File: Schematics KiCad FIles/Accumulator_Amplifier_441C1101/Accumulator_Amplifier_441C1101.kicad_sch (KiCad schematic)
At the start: 22 parts, among them J1 Edge, U1101 5963, U1105 5963

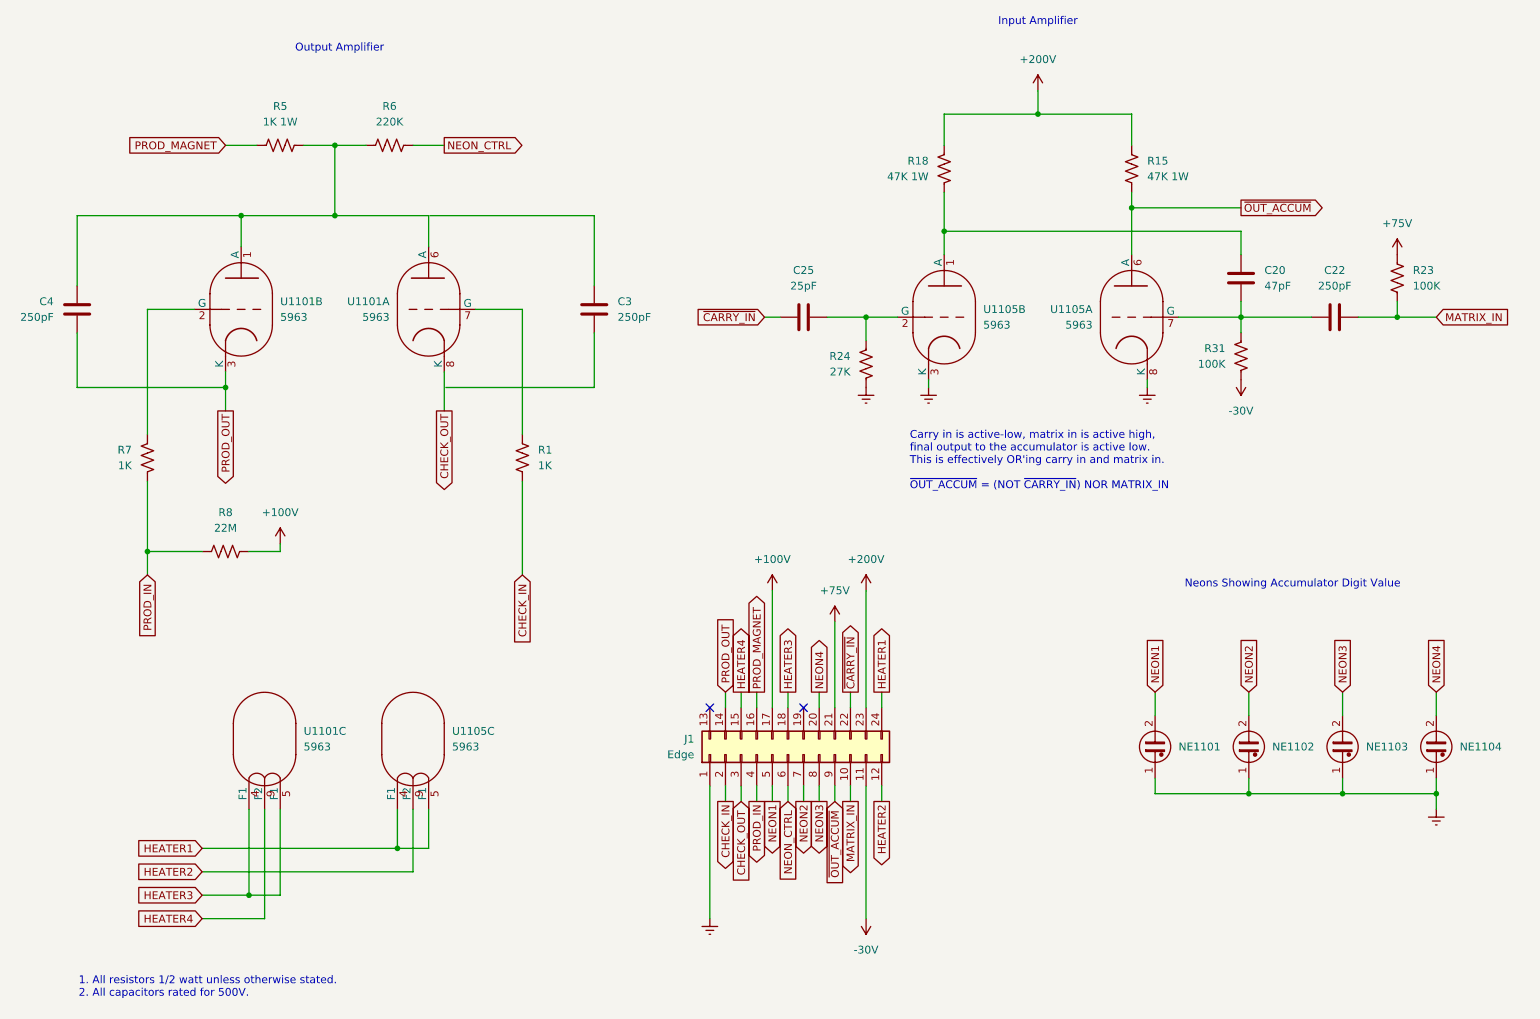
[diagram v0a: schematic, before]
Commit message: Fix component designators on accumulator schematics
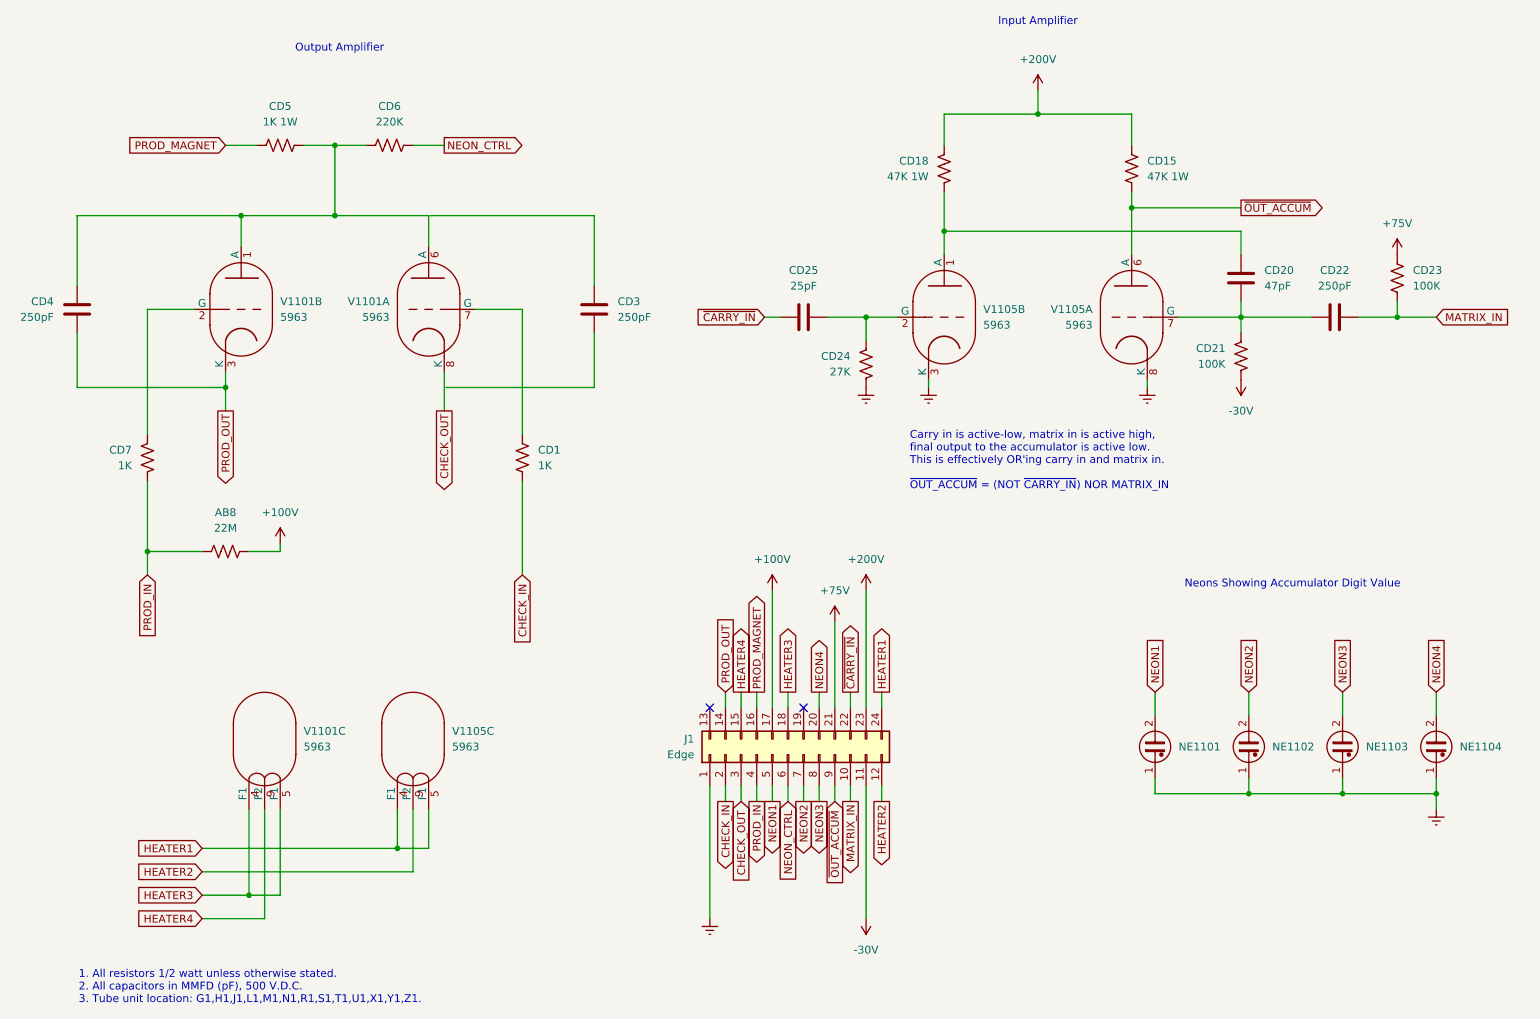
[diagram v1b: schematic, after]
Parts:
- renumbered R8 to AB8, R1 to CD1, R15 to CD15, R18 to CD18, C20 to CD20, R31 to CD21, C22 to CD22, R23 to CD23, R24 to CD24, C25 to CD25, C3 to CD3, C4 to CD4, R5 to CD5, R6 to CD6, R7 to CD7, U1101 to V1101, U1105 to V1105
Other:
- note added: "1. All resistors 1/2 watt unless otherwise stated. 2. All capacitors in MMFD (pF), 500 V.D.C. 3. Tube unit location: G1,H1,J1,L1,M1,N1,R1,S1,T1,U1,X1,Y1,Z1."
- note removed: "1. All resistors 1/2 watt unless otherwise stated. 2. All capacitors rated for 500V."
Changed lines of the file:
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@@
 		(title "Compu-Tronic Accumulator Amplifier Schematic")
 		(date "11-4-1958")
+		(comment 2 "For wiring diagram see 441E1102")
 	)
 	(junction
@@
 		)
 	)
-	(text "1. All resistors 1/2 watt unless otherwise stated.\n2. All capacitors rated for 500V."
+	(text "1. All resistors 1/2 watt unless otherwise stated.\n2. All capacitors in MMFD (pF), 500 V.D.C.\n3. Tube unit location: G1,H1,J1,L1,M1,N1,R1,S1,T1,U1,X1,Y1,Z1."
 		(exclude_from_sim no)
 		(at 32.004 178.816 0)
@@
 		(on_board yes)
 		(dnp no)
-		(property "Reference" "U1101"
+		(property "Reference" "V1101"
 			(at 82.55 67.3099 0)
 			(effects
@@
 			(project "Input_Amplifiier"
 				(path "/519d7692-6bf3-45ab-bd58-713783b63e8a"
-					(reference "U1101")
+					(reference "V1101")
 					(unit 1)
 				)
@@
 		(on_board yes)
 		(dnp no)
-		(property "Reference" "R23"
+		(property "Reference" "CD23"
 			(at 248.92 62.2299 0)
 			(effects
@@
 			(project "Accumulator_Amplifier_441C1101"
 				(path "/519d7692-6bf3-45ab-bd58-713783b63e8a"
-					(reference "R23")
+					(reference "CD23")
 					(unit 1)
 				)
@@
 		(dnp no)
 		(fields_autoplaced yes)
-		(property "Reference" "R8"
+		(property "Reference" "AB8"
 			(at 55.88 101.6 90)
 			(effects
@@
 			(project ""
 				(path "/519d7692-6bf3-45ab-bd58-713783b63e8a"
-					(reference "R8")
+					(reference "AB8")
 					(unit 1)
 				)
@@
 		(dnp no)
 		(fields_autoplaced yes)
-		(property "Reference" "R5"
+		(property "Reference" "CD5"
 			(at 64.77 35.56 90)
 			(effects
@@
 			(project "Accumulator_Amplifier_441C1101"
 				(path "/519d7692-6bf3-45ab-bd58-713783b63e8a"
-					(reference "R5")
+					(reference "CD5")
 					(unit 1)
 				)
@@
 		(on_board yes)
 		(dnp no)
-		(property "Reference" "C3"
+		(property "Reference" "CD3"
 			(at 119.634 67.3099 0)
 			(effects
@@
 			(project "Accumulator_Amplifier_441C1101"
 				(path "/519d7692-6bf3-45ab-bd58-713783b63e8a"
-					(reference "C3")
+					(reference "CD3")
 					(unit 1)
 				)
@@
 		(on_board yes)
 		(dnp no)
-		(property "Reference" "C20"
+		(property "Reference" "CD20"
 			(at 224.79 62.2299 0)
 			(effects
@@
 			(project "Accumulator_Amplifier_441C1101"
 				(path "/519d7692-6bf3-45ab-bd58-713783b63e8a"
-					(reference "C20")
+					(reference "CD20")
 					(unit 1)
 				)
@@
 		(on_board yes)
 		(dnp no)
-		(property "Reference" "R31"
+		(property "Reference" "CD21"
 			(at 218.44 74.9299 0)
 			(effects
@@
 			(project "Accumulator_Amplifier_441C1101"
 				(path "/519d7692-6bf3-45ab-bd58-713783b63e8a"
-					(reference "R31")
+					(reference "CD21")
 					(unit 1)
 				)
@@
 		(on_board yes)
 		(dnp no)
-		(property "Reference" "R7"
+		(property "Reference" "CD7"
 			(at 40.64 91.4399 0)
 			(effects
@@
 			(project ""
 				(path "/519d7692-6bf3-45ab-bd58-713783b63e8a"
-					(reference "R7")
+					(reference "CD7")
 					(unit 1)
 				)
@@
 		(dnp no)
 		(fields_autoplaced yes)
-		(property "Reference" "U1101"
+		(property "Reference" "V1101"
 			(at 68.58 137.1599 0)
 			(effects
@@
 			(project "Input_Amplifiier"
 				(path "/519d7692-6bf3-45ab-bd58-713783b63e8a"
-					(reference "U1101")
+					(reference "V1101")
 					(unit 3)
 				)
@@
 		(on_board yes)
 		(dnp no)
-		(property "Reference" "R15"
+		(property "Reference" "CD15"
 			(at 205.74 44.4499 0)
 			(effects
@@
 			(project "Accumulator_Amplifier_441C1101"
 				(path "/519d7692-6bf3-45ab-bd58-713783b63e8a"
-					(reference "R15")
+					(reference "CD15")
 					(unit 1)
 				)
@@
 		(on_board yes)
 		(dnp no)
-		(property "Reference" "U1105"
+		(property "Reference" "V1105"
 			(at 196.85 68.5799 0)
 			(effects
@@
 			(project ""
 				(path "/519d7692-6bf3-45ab-bd58-713783b63e8a"
-					(reference "U1105")
+					(reference "V1105")
 					(unit 1)
 				)
@@
 		(dnp no)
 		(fields_autoplaced yes)
-		(property "Reference" "U1105"
+		(property "Reference" "V1105"
 			(at 92.71 137.1599 0)
 			(effects
@@
 			(project ""
 				(path "/519d7692-6bf3-45ab-bd58-713783b63e8a"
-					(reference "U1105")
+					(reference "V1105")
 					(unit 3)
 				)
@@
 		(dnp no)
 		(fields_autoplaced yes)
-		(property "Reference" "C22"
+		(property "Reference" "CD22"
 			(at 236.22 62.23 90)
 			(effects
@@
 			(project "Accumulator_Amplifier_441C1101"
 				(path "/519d7692-6bf3-45ab-bd58-713783b63e8a"
-					(reference "C22")
+					(reference "CD22")
 					(unit 1)
 				)
@@
 		(on_board yes)
 		(dnp no)
-		(property "Reference" "R24"
+		(property "Reference" "CD24"
 			(at 157.48 76.1999 0)
 			(effects
@@
 			(project "Accumulator_Amplifier_441C1101"
 				(path "/519d7692-6bf3-45ab-bd58-713783b63e8a"
-					(reference "R24")
+					(reference "CD24")
 					(unit 1)
 				)
@@
 		(on_board yes)
 		(dnp no)
-		(property "Reference" "R18"
+		(property "Reference" "CD18"
 			(at 170.18 44.4499 0)
 			(effects
@@
 			(project "Accumulator_Amplifier_441C1101"
 				(path "/519d7692-6bf3-45ab-bd58-713783b63e8a"
-					(reference "R18")
+					(reference "CD18")
 					(unit 1)
 				)
@@
 		(dnp no)
 		(fields_autoplaced yes)
-		(property "Reference" "R6"
+		(property "Reference" "CD6"
 			(at 82.55 35.56 90)
 			(effects
@@
 			(project "Accumulator_Amplifier_441C1101"
 				(path "/519d7692-6bf3-45ab-bd58-713783b63e8a"
-					(reference "R6")
+					(reference "CD6")
 					(unit 1)
 				)
@@
 		(on_board yes)
 		(dnp no)
-		(property "Reference" "C4"
+		(property "Reference" "CD4"
 			(at 27.94 67.3099 0)
 			(effects
@@
 			(project ""
 				(path "/519d7692-6bf3-45ab-bd58-713783b63e8a"
-					(reference "C4")
+					(reference "CD4")
 					(unit 1)
 				)
@@
 		(dnp no)
 		(fields_autoplaced yes)
-		(property "Reference" "U1101"
+		(property "Reference" "V1101"
 			(at 64.77 67.3099 0)
 			(effects
@@
 			(project "Input_Amplifiier"
 				(path "/519d7692-6bf3-45ab-bd58-713783b63e8a"
-					(reference "U1101")
+					(reference "V1101")
 					(unit 2)
 				)
@@
 		(dnp no)
 		(fields_autoplaced yes)
-		(property "Reference" "C25"
+		(property "Reference" "CD25"
 			(at 149.86 62.23 90)
 			(effects
@@
 			(project ""
 				(path "/519d7692-6bf3-45ab-bd58-713783b63e8a"
-					(reference "C25")
+					(reference "CD25")
 					(unit 1)
 				)
@@
 		(on_board yes)
 		(dnp no)
-		(property "Reference" "R1"
+		(property "Reference" "CD1"
 			(at 106.68 91.4399 0)
 			(effects
@@
 			(project "Accumulator_Amplifier_441C1101"
 				(path "/519d7692-6bf3-45ab-bd58-713783b63e8a"
-					(reference "R1")
+					(reference "CD1")
 					(unit 1)
 				)
@@
 		(dnp no)
 		(fields_autoplaced yes)
-		(property "Reference" "U1105"
+		(property "Reference" "V1105"
 			(at 179.07 68.5799 0)
 			(effects
@@
 			(project ""
 				(path "/519d7692-6bf3-45ab-bd58-713783b63e8a"
-					(reference "U1105")
+					(reference "V1105")
 					(unit 2)
 				)
